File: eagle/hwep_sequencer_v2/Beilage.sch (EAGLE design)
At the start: 142 parts, among them X1 ESP32-AZDEL

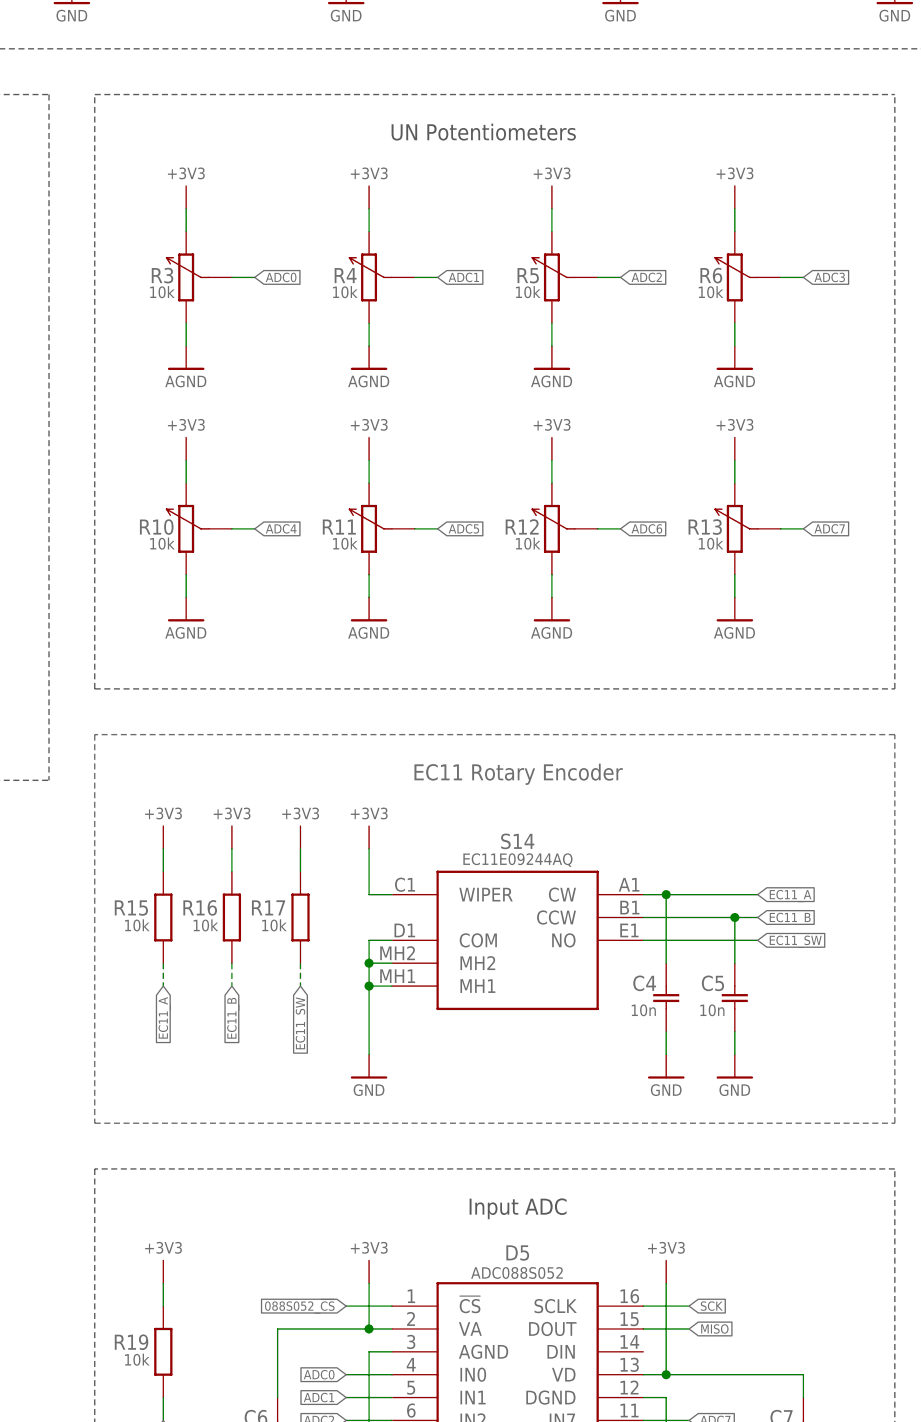
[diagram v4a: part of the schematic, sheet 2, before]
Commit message: fixed traces
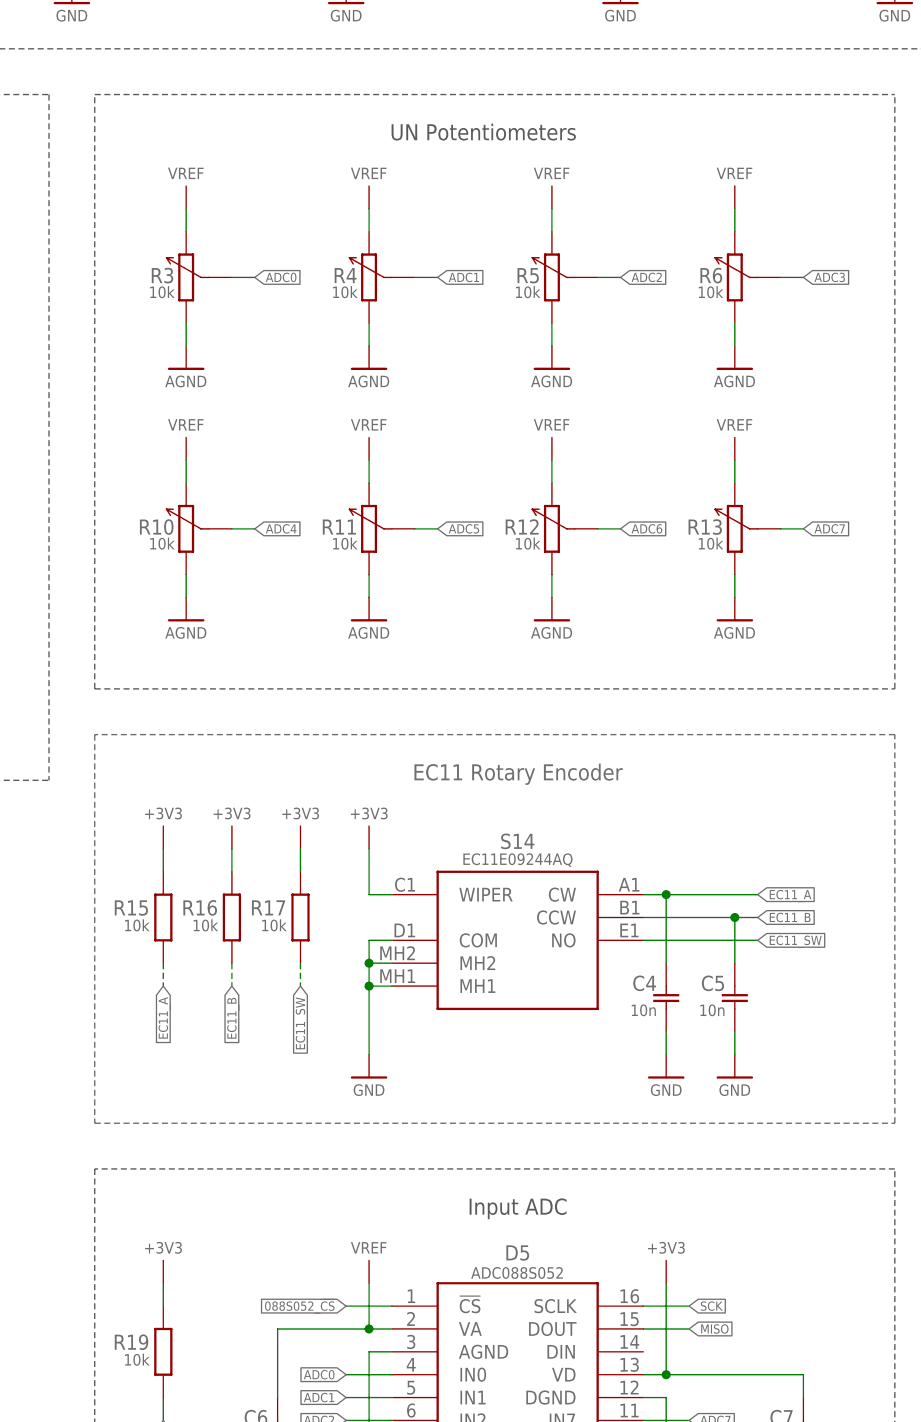
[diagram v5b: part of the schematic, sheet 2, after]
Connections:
- new net !CS!_C: D4.C, X1.GPIO22
- new net VREF: C6.1, D5.VA, R10.2, R11.2, R12.2, R13.2, R3.2, R4.2, R5.2, R6.2
- net +3V3: no longer C6.1, D5.VA, R10.2, R11.2, R12.2, R13.2, R3.2, R4.2, R5.2, R6.2

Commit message: Documentation Update
Added STL
cleaned up docs
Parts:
- D6, D7, D8: CATEGORY (none) -> 13
- H10, H11, H12, H13, H14, H3, H4, H5, H6, H7, H8, H9: CATEGORY (none) -> 7
- R10, R11, R12, R13, R3, R4, R5, R6: device rcl_GruS:P160L -> rcl_GruS:P160LB
- X1: value ESP32-AZDEL -> ESP32-DEVKIT-C; device modul_GruS:ESP32-AZDEL -> modul_GruS:ESP32-DEVKIT-C
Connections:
- net +3V3: no longer S14.WIPER
- net 7SEG_CE: now also R28.2, V1.G, X1.GPIO26/ADC2_CH9/DAC2; no longer R30.2, V3.G, X1.GPIO33/ADC1_CH5
- net 7SEG_CH: now also R30.2, V3.G, X1.GPIO33/ADC1_CH5; no longer R28.2, V1.G, X1.GPIO26/ADC2_CH9/DAC2
- net GND: now also S14.WIPER
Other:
- note added: "Potentiometer Shaft Length is 25mm"
- note removed: "-?- Eigene Referenzspannung für Analog -?- Spannungsversorgung"

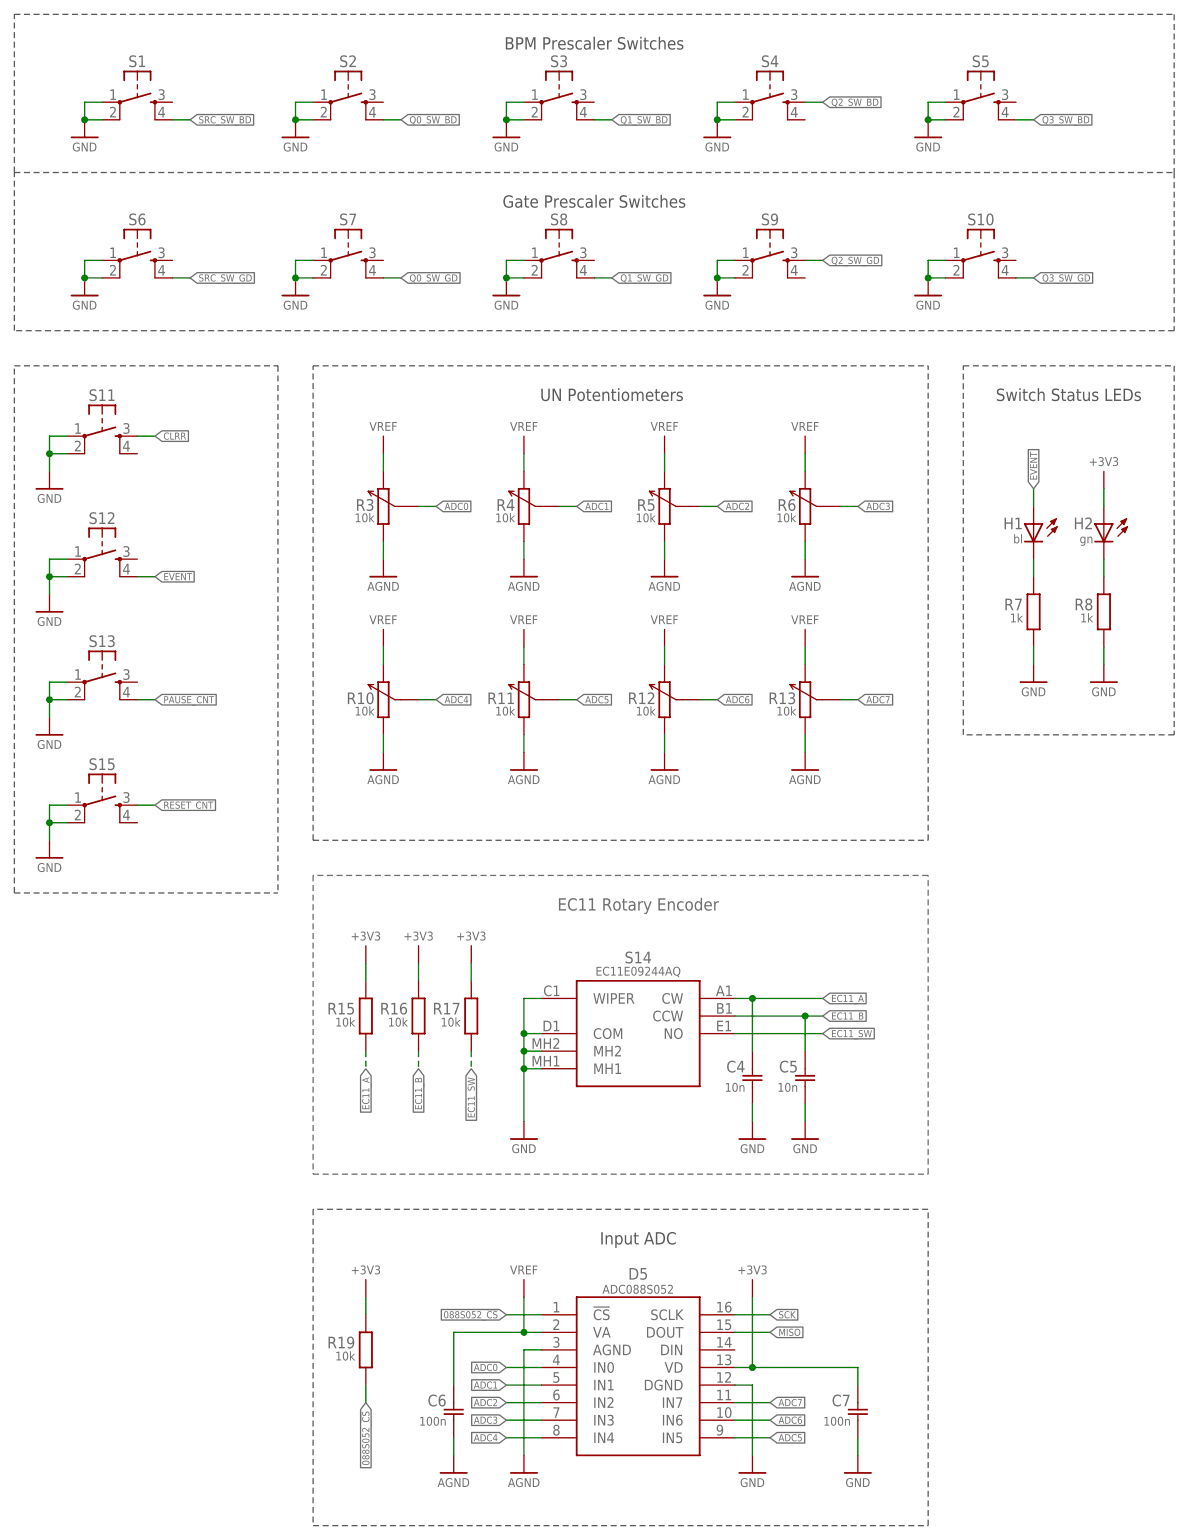
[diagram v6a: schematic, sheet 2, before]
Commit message: Prescaler Sim
Optimised Schematic
Changed unavailable ICs
Issue: Interrupt on Input MCP23S08 and Prescaler Strobe
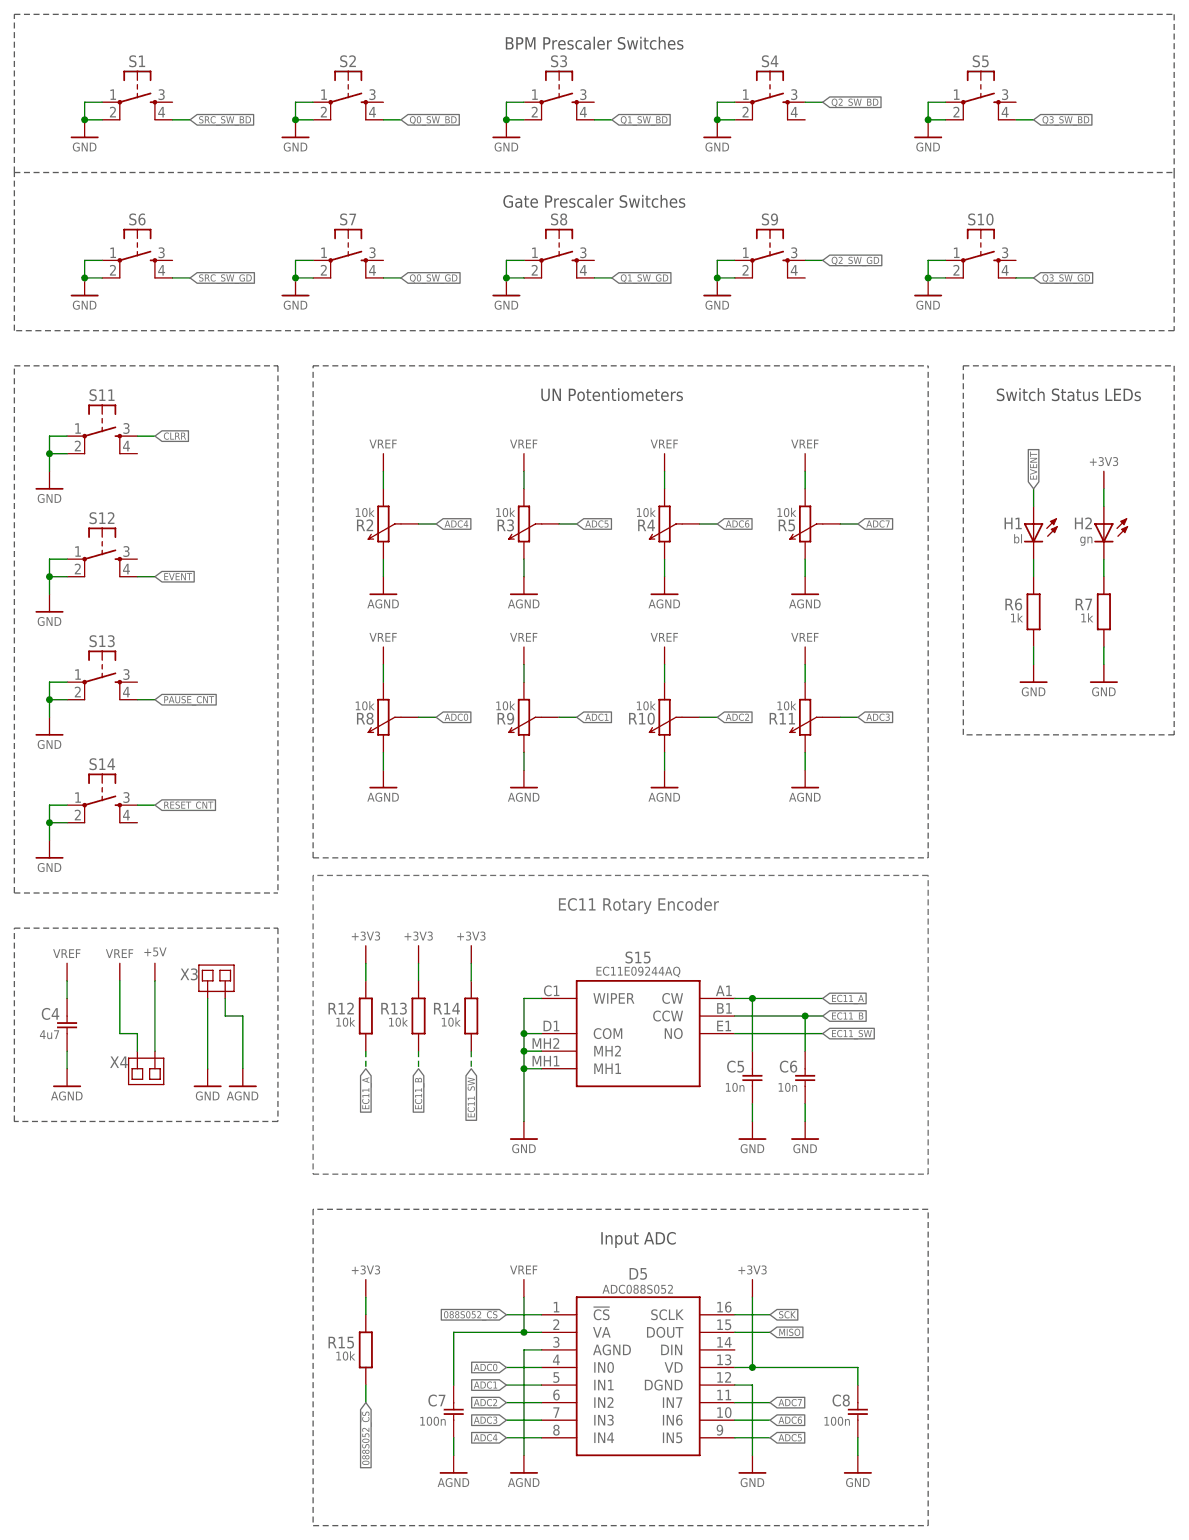
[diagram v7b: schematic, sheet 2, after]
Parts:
- removed R31, R33: 10k, rcl_GruS:R-EUSR0805
- removed R32, R34: 2k7, rcl_GruS:R-EUSR0805
- added C31: 100n, rcl_GruS:C-EUC0805
- added R14: 10k, rcl_GruS:R-EUSR0805
- added R18: 100R, rcl_GruS:R-EU_R0805
- added R2, R9: 10k, rcl_GruS:P160LB
- added X3, X4: (no value), con_GruS:JUMPSMD1FACH-1
- C10, C25, C29: value 100n -> 1u
- C23, C27, C8: value 1u -> 100n
- C4: value 10n -> 4u7; CATEGORY 2 -> (none)
- C6: value 100n -> 10n
- D11, D13: value 74AHC1G04DBV -> 74AHC1G125DBV; device 74xx_GruS:74AHC1G04DBV -> 74xx_GruS:74AHC1G125DBV
- D9: value 74AHCT1G125DBV -> 74AHC1G125DBV; device 74xx_GruS:74AHCT1G125DBV -> 74xx_GruS:74AHC1G125DBV
- R12, R13: device rcl_GruS:P160LB -> rcl_GruS:R-EUSR0805
- R16, R17, R19: value 10k -> 100R; device rcl_GruS:R-EUSR0805 -> rcl_GruS:R-EU_R0805
- R24, R25, R26: value 100R -> 100k; device rcl_GruS:R-EU_R0805 -> rcl_GruS:R-EUSR0805
- R27: value 100R -> 10k; device rcl_GruS:R-EU_R0805 -> rcl_GruS:R-EUSR0805
- R28, R30: value 100k -> 2k7
- R29: value 100k -> 10k
- R6: value 10k -> 1k; device rcl_GruS:P160LB -> rcl_GruS:R-EUSR0805
- R8: value 1k -> 10k; device rcl_GruS:R-EUSR0805 -> rcl_GruS:P160LB
- S14: value EC11E09244AQ -> (none); device switch_GruS:EC11E09244AQ -> switch_GruS:TASTE10XX
- S15: value (none) -> EC11E09244AQ; device switch_GruS:TASTE10XX -> switch_GruS:EC11E09244AQ
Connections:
- removed net N$1: D6.EO, D7.EI
- new net INT_23S08: D1.INT
- new net PSGS: D8D.Y
- net +3V3: now also C10.1, C31.1, D11G$1.A, D11P.VCC, D13G$1.A, D13P.VCC, R12.2, R13.2, R14.2; no longer C23.1, C7.1, D11G$2.VCC, D13G$2.VCC, R16.2, R17.2, R19.2, R31.2, R33.2
- net +5V: now also C23.1, X4.1; no longer C10.1
- net 088S052_!CS!: now also R15.1; no longer R19.1
- net 7SEG_A: now also R23.2; no longer R27.2
- net 7SEG_B: now also R22.2; no longer R26.2
- net 7SEG_C: now also R21.2; no longer R25.2
- net 7SEG_CE: now also R24.2; no longer R28.2
- net 7SEG_CH: now also R26.2; no longer R30.2
- net 7SEG_CZ: now also R25.2; no longer R29.2
- net 7SEG_D: now also R20.2; no longer R24.2
- net 7SEG_DP: now also R16.2; no longer R20.2
- net 7SEG_E: now also R19.2; no longer R23.2
- net 7SEG_F: now also R18.2; no longer R22.2
- net 7SEG_G: now also R17.2; no longer R21.2
- net ADC0: now also R8.3; no longer R3.3
- net ADC1: now also R9.3; no longer R4.3
- net ADC2: now also R10.3; no longer R5.3
- net ADC3: now also R11.3; no longer R6.3
- net ADC4: now also R2.3; no longer R10.3
- net ADC5: now also R3.3; no longer R11.3
- net ADC6: now also R4.3; no longer R12.3
- net ADC7: now also R5.3; no longer R13.3
- net AGND: now also C4.2, C7.2, R10.2, R11.2, R2.2, R3.2, R4.2, R5.2, R8.2, R9.2, X3.2; no longer C6.2, R10.1, R11.1, R12.1, R13.1, R3.1, R4.1, R5.1, R6.1
- net EC11_A: now also C5.1, R12.1, S15.CW; no longer C4.1, R15.1, S14.CW
- net EC11_B: now also C6.1, R13.1, S15.CCW; no longer C5.1, R16.1, S14.CCW
- net EC11_SW: now also R14.1, S15.NO; no longer R17.1, S14.NO
- net GND: now also C31.2, C6.2, D11P.GND, D13P.GND, R24.1, R25.1, R26.1, R27.1, R6.1, S14.P, S14.P1, S15.COM, S15.MH1, S15.MH2, S15.WIPER, X3.1; no longer C4.2, C7.2, D11G$2.GND, D13G$2.GND, R32.1, R34.1, R8.1, S14.COM, S14.MH1, S14.MH2, S14.WIPER, S15.P, S15.P1
- net N$24: now also R28.2; no longer R32.2
- net N$33: now also R17.1; no longer R21.1
- net N$35: now also R18.1; no longer R22.1
- net N$36: now also R23.1; no longer R27.1
- net N$37: now also R22.1; no longer R26.1
- net N$54: now also R30.2; no longer R34.2
- net N$56: now also R20.1; no longer R24.1
- net N$58: now also R6.2; no longer R7.2
- net N$61: now also R29.2; no longer R33.1
- net N$66: now also R27.2; no longer R31.1
- net N$7: now also R16.1; no longer R20.1
- net N$78: now also R21.1; no longer R25.1
- net N$80: now also R19.1; no longer R23.1
- net N$9: now also R7.2; no longer R8.2
- net PS3: now also D6.EO, D7.EI; no longer D8D.Y
- net RESET_CNT: now also S14.S; no longer S15.S
- net STP_LE_K: now also D11G$1.!OE; no longer D11G$1.A
- net STP_LE_S: now also D13G$1.!OE; no longer D13G$1.A
- net VREF: now also C4.1, C7.1, R10.1, R11.1, R2.1, R3.1, R4.1, R5.1, R8.1, R9.1, X4.2; no longer C6.1, R10.2, R11.2, R12.2, R13.2, R3.2, R4.2, R5.2, R6.2
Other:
- moved on the sheet: C1, C11, C12, C13, C14, C15, C16, C17, C18, C19, C20, C21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

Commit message: i2s testing & KUB
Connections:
- new net N$1: X2.1
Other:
- moved on the sheet: X2
